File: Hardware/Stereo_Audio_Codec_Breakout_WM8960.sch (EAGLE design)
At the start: 63 parts, among them J1 QWIIC, U4 WM8960, U5 LM1117, Y1 24 MHz

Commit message: moved pwr led into sch frame
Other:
- note removed: "Power LED"
- moved on the sheet: D1, LED, R5

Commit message: Switched MONO OUT to OUT3, because that is a better name
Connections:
- removed net MONO_OUT: J3.8, U4.MONO_OUT
- new net OUT3: J3.8, U4.OUT3
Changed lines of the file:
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@@
 </segment>
 </net>
-<net name="MONO_OUT" class="0">
+<net name="OUT3" class="0">
 <segment>
-<pinref part="U4" gate="G$1" pin="MONO_OUT"/>
+<pinref part="U4" gate="G$1" pin="OUT3"/>
 <wire x1="114.3" y1="154.94" x2="116.84" y2="154.94" width="0.1524" layer="91"/>
 <label x="116.84" y="154.94" size="1.27" layer="95" font="vector" xref="yes"/>

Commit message: Switched to single GND plane
-moved to smaller vreg for AVDD
-changed how power jumpers selection and isolation works
-created 3.3V and AVDD polygons on inner layers
-increased header length to allow for 100% analog pins to be on same side.
-split SPKVDD decoupling cap into two separate 4.7uF caps and put near IC pins
-added 10 ohm in series resistors on all data lines.
-moved input filtering passives closer to IC pins
-moved SPK filtering passive closer to IC pins
-updated all silk
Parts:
- removed AVDD: JUMPER-SMT_3_1-NC_TRACE_SILK, SparkFun-Jumpers:JUMPER-SMT_3_1-NC_TRACE_SILK
- removed C11: 10uF, SparkFun-Capacitors:10UF-0805-25V-10%
- removed C2: 10uF, SparkFun-Capacitors:10UF-0402T-6.3V-20%
- removed FB1, FB2, FB3: 600Ω, SparkFun-Coils:FERRITE_BEAD-0805-600Ω-100MHZ
- removed FRAME2: FRAME-LETTER, SparkFun-Aesthetics:FRAME-LETTER
- removed J2, J3: (no value), SparkFun-Connectors:CONN_14NO_SILK
- removed R11: 240, SparkFun-Resistors:240OHM-0603-1/10W-1%
- removed U5: LM1117, SparkFun-IC-Power:V_REG_LM1117SOT223
- added AVDD-ISO: JUMPER-SMT_2_NC_TRACE_SILK, SparkFun-Jumpers:JUMPER-SMT_2_NC_TRACE_SILK
- added C12: 1.0uF, SparkFun-Capacitors:1.0UF-0402T-16V-10%
- added C14, C31: 10uF, SparkFun-Capacitors:10UF-0402T-6.3V-20%
- added C6, C7: 4.7uF, SparkFun-Capacitors:4.7UF0603
- added FRAME1: FRAME-LEDGER, SparkFun-Aesthetics:FRAME-LEDGER
- added J4, J5: (no value), SparkFun-Connectors:CONN_161X16_NO_SILK
- added R13, R14, R15, R16, R17: 10Ω, SparkFun-Resistors:10OHM-0402-1/16W-5%
- added R18: 100k, SparkFun-Resistors:100KOHM-0402T-1/16W-1%
- added U3: XC6222B331MR-G, SparkFun-IC-Power:XC6222B331MR-G
- I2C: value JUMPER-SMT_3_2-NC_TRACE_NO-SILK -> JUMPER-SMT_3_2-NC_TRACE_SILK; device SparkFun-Jumpers:JUMPER-SMT_3_2-NC_TRACE_NO-SILK -> SparkFun-Jumpers:JUMPER-SMT_3_2-NC_TRACE_SILK
- LOGO1: value SFE_LOGO_NAME_FLAMEBLANK -> SFE_LOGO_NAME_FLAME.1_INCH; device SparkFun-Aesthetics:SFE_LOGO_NAME_FLAMEBLANK -> SparkFun-Aesthetics:SFE_LOGO_NAME_FLAME.1_INCH
- R10: value 390 -> 10Ω; device SparkFun-Resistors:390OHM-0603-1/10W-1% -> SparkFun-Resistors:10OHM-0402-1/16W-5%
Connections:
- removed net AGND: C1.2, C10.1, C15.2, C16.2, C17.2, C18.2, C2.2, C21.2, C22.2, C27.2, C28.2, C29.2, C30.2, C8.1, C9.1, FB1.1, J2.11, J3.6, R10.1, U4.AGND, U4.GNDPADDLE
- removed net DGND: C11.2, C13.2, C3.1, C4.1, C5.1, FB1.2, J1.1, J2.1, R5.1, U4.DGND, U4.SPKGND1, U4.SPKGND2, Y1.GND
- removed net N$45: C1.1, FB2.2, U5.IN
- new net EN: J4.3, R18.2, U3.EN
- new net GND: C1.2, C10.1, C12.2, C13.2, C14.2, C15.2, C16.2, C17.2, C18.2, C21.2, C22.2, C27.2, C28.2, C29.2, C3.1, C30.2, C31.2, C4.1, C5.1, C6.2, C7.2, C8.1, C9.1, J1.1, J4.1, J4.16, J4.2, J4.6, J5.16, R5.1, U3.GND, U4.AGND, U4.DGND, U4.GNDPADDLE, U4.SPKGND1, U4.SPKGND2, Y1.GND
- new net N$21: R14.2, U4.DACLRC
- new net N$22: R15.2, U4.BCLK
- new net N$23: R16.2, U4.ADCDAT
- new net N$24: R17.2, U4.DACDAT
- net 3.3V: now also J4.8, SPKVDD.1; no longer FB3.2, J2.2, SPKVDD.3
- net ADCDAT: now also J4.11, R16.1; no longer J2.5, U4.ADCDAT
- net ADCLRC: now also J4.12, R13.1; no longer J2.6, U4.ADCLRC/GPIO
- net AVDD: now also AVDD-ISO.2, J5.5; no longer AVDD.2, J3.10
- net AVDD-REG: now also AVDD-ISO.1, C12.1, C14.1, U3.OUT; no longer AVDD.3, C2.1, R11.2, U5.OUT
- net BCLK: now also J4.15, R15.1; no longer J2.9, U4.BCLK
- net DACDAT: now also J4.13, R17.1; no longer J2.7, U4.DACDAT
- net DACLRC: now also J4.14, R14.1; no longer J2.8, U4.DACLRC
- net HP_L: now also J5.8; no longer J3.9
- net HP_R: now also J5.6; no longer J3.7
- net LINPUT1: now also J5.12; no longer J3.14
- net LINPUT2: now also J5.11; no longer J3.13
- net LINPUT3: now also J5.10; no longer J3.12
- net MICBIAS: now also J5.9; no longer J3.11
- net N$11: now also R10.1; no longer U4.MCLK
- net N$2: now also R13.2, U4.ADCLRC/GPIO; no longer AVDD.1, FB3.1
- net N$25: now also U4.MCLK; no longer R11.1, U5.ADJ
- net OUT3: now also J5.7; no longer J3.8
- net RINPUT1: now also J5.13; no longer J2.14
- net RINPUT2: now also J5.14; no longer J2.13
- net RINPUT3: now also J5.15; no longer J2.12
- net SCL: now also J4.10; no longer J2.4
- net SDA: now also J4.9; no longer J2.3
- net SPKVDD: now also C6.1, C7.1, J4.5; no longer C11.1, J3.1
- net SPK_LN: now also J5.3; no longer J3.4
- net SPK_LP: now also J5.4; no longer J3.5
- net SPK_RN: now also J5.1; no longer J3.2
- net SPK_RP: now also J5.2; no longer J3.3
- net VIN: now also C1.1, C31.1, J4.4, R18.1, SPKVDD.3, U3.IN; no longer FB2.1, J2.10, SPKVDD.1
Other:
- note added: "700mA out 6V max in"
- note added: "Cut AVDD-ISO Jumper To isolate AVDD from U3, And then provide AVDD at header pin."
- note added: "Power LED"
- note added: "Speaker VDD Source Selection Jumper"
- note added: "Supply Voltage Ranges VIN: 3.7-5.5V* DCVDD: 1.7-3.6V DBVDD: 1.7-3.6V AVDD: 2.7-3.6V SPKVDD: 2.7-5.5V * If VIN is used for SPKVDD, then VIN shouold be limited to 5.5V by SPKVDD max range"
- note added: "Use SPKVDD Jumper To select SPKVDD source. Leave both open to provide external SPKVDD at Header pin."
- note removed: "Power Selection Jumpers"
- note removed: "Supply Voltage Ranges DCVDD: 1.7-3.6V DBVDD: 1.7-3.6V AVDD: 2.7-3.6V SPKVDD: 2.7-5.5V"
- moved on the sheet: C1, C10, C13, C15, C16, C17, C18, C19, C20, C21, C22, C23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

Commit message: checklist catches - eng run
-Connected header pin (J4/7) to GND
-Added 4-layer board 1/2/3/4 in copper
-added ordering instructions
-added Selective solder path and moved some resistors to provide clearance on medium nozzle
-nudges some Vias to avoid cutting into silk
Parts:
- added LOGO5: SPECIAL_INSTRUCTIONS-ORDERING, SparkFun-Aesthetics:SPECIAL_INSTRUCTIONS-ORDERING
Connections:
- net GND: now also J4.7
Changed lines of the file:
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@@
 <part name="SUPPLY7" library="SparkFun-PowerSymbols" deviceset="3.3V" device=""/>
 <part name="FRAME1" library="SparkFun-Aesthetics" deviceset="FRAME-LEDGER" device=""/>
+<part name="LOGO5" library="SparkFun-Aesthetics" deviceset="SPECIAL_INSTRUCTIONS" device="-ORDERING"/>
 </parts>
 <sheets>
@@
 <attribute name="REV" x="419.1" y="6.604" size="2.7432" layer="94" font="vector"/>
 </instance>
+<instance part="LOGO5" gate="G$1" x="281.94" y="22.86" smashed="yes"/>
 </instances>
 <busses>
@@
 <wire x1="66.04" y1="101.6" x2="63.5" y2="101.6" width="0.1524" layer="91"/>
 <junction x="66.04" y="76.2"/>
-<wire x1="66.04" y1="76.2" x2="66.04" y2="101.6" width="0.1524" layer="91"/>
+<wire x1="66.04" y1="76.2" x2="66.04" y2="78.74" width="0.1524" layer="91"/>
+<wire x1="66.04" y1="78.74" x2="66.04" y2="101.6" width="0.1524" layer="91"/>
 <wire x1="66.04" y1="63.5" x2="63.5" y2="63.5" width="0.1524" layer="91"/>
 <junction x="66.04" y="63.5"/>
@@
 <wire x1="66.04" y1="66.04" x2="63.5" y2="66.04" width="0.1524" layer="91"/>
 <junction x="66.04" y="66.04"/>
-</segment>
-<segment>
+<pinref part="J4" gate="G$1" pin="7"/>
+<wire x1="66.04" y1="78.74" x2="63.5" y2="78.74" width="0.1524" layer="91"/>
+<junction x="66.04" y="78.74"/>
+</segment>
+<segment>

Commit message: corrected typo in sch note about I2C pullup jumper
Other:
- note added: "Cut I2C Jumpers to remove pullup resistors from the I2C bus."
- note removed: "Cut I2C Jumper to remove pullup jumpers from the I2C bus."
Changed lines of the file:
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@@
 <text x="348.742" y="11.43" size="2.54" layer="94" font="vector">Pete Lewis</text>
 <text x="7.62" y="271.78" size="3.81" layer="94" font="vector" ratio="10">Audio Codec</text>
-<text x="370.84" y="106.68" size="1.778" layer="97" font="vector">Cut I2C Jumper to
-remove pullup jumpers
+<text x="370.84" y="106.68" size="1.778" layer="97" font="vector">Cut I2C Jumpers to
+remove pullup resistors
 from the I2C bus.</text>
 <text x="421.64" y="7.62" size="2.54" layer="94" font="vector">v01</text>

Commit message: Silk updates and codec package update
-corrected the I2S pins to be rounded flags (because they can be inputs or outputs)
-extended pads on codec FP to allow for better fillets. (also increased roundness of pads)
-corrected I2C address in schematic to 0x1A
-bumped version to v10
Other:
- note added: "I2C Address: 0x1A (unshifted)"
- note added: "v10"
- note removed: "I2C Address: 0x34 (unshifted)"
- note removed: "v01"
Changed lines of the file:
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@@
 remove pullup resistors
 from the I2C bus.</text>
-<text x="421.64" y="7.62" size="2.54" layer="94" font="vector">v01</text>
+<text x="421.64" y="7.62" size="2.54" layer="94" font="vector">v10</text>
 <text x="331.978" y="6.858" size="1.778" layer="94" font="vector">Based on the Top pHAT by Andy England</text>
-<text x="76.708" y="169.418" size="1.778" layer="97" font="vector">I2C Address: 0x34 (unshifted)</text>
+<text x="76.708" y="169.418" size="1.778" layer="97" font="vector">I2C Address: 0x1A (unshifted)</text>
 <text x="238.76" y="93.98" size="1.27" layer="97" font="vector">Cut LED Jumper
 to disable power LED</text>

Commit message: replaced C6 and C7 to use proper SFE libraries
-Also updated tCream on codec footprint
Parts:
- C6, C7: device SparkFun-Capacitors:4.7UF0603 -> SparkFun-Capacitors:4.7UF-0603-6.3V-(10%)
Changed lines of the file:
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@@
 <part name="SUPPLY14" library="SparkFun-PowerSymbols" deviceset="5V" device="" value="SPKVDD"/>
 <part name="LOGO1" library="SparkFun-Aesthetics" deviceset="SFE_LOGO_NAME_FLAME" device=".1_INCH" value="SFE_LOGO_NAME_FLAME.1_INCH"/>
-<part name="C6" library="SparkFun-Capacitors" library_urn="urn:adsk.eagle:library:510" deviceset="4.7UF" device="0603" package3d_urn="urn:adsk.eagle:package:37414/1" value="4.7uF"/>
-<part name="C7" library="SparkFun-Capacitors" library_urn="urn:adsk.eagle:library:510" deviceset="4.7UF" device="0603" package3d_urn="urn:adsk.eagle:package:37414/1" value="4.7uF"/>
+<part name="C6" library="SparkFun-Capacitors" deviceset="4.7UF" device="-0603-6.3V-(10%)" value="4.7uF"/>
+<part name="C7" library="SparkFun-Capacitors" deviceset="4.7UF" device="-0603-6.3V-(10%)" value="4.7uF"/>
 <part name="R13" library="SparkFun-Resistors" deviceset="10OHM" device="-0402-1/16W-5%" value="10Ω"/>
 <part name="R14" library="SparkFun-Resistors" deviceset="10OHM" device="-0402-1/16W-5%" value="10Ω"/>
@@
 which will not be processed correctly with this version.
 </note>
-<note version="8.2" severity="warning">
-Since Version 8.2, EAGLE supports online libraries. The ids
-of those online libraries will not be understood (or retained)
-with this version.
-</note>
 <note version="8.3" severity="warning">

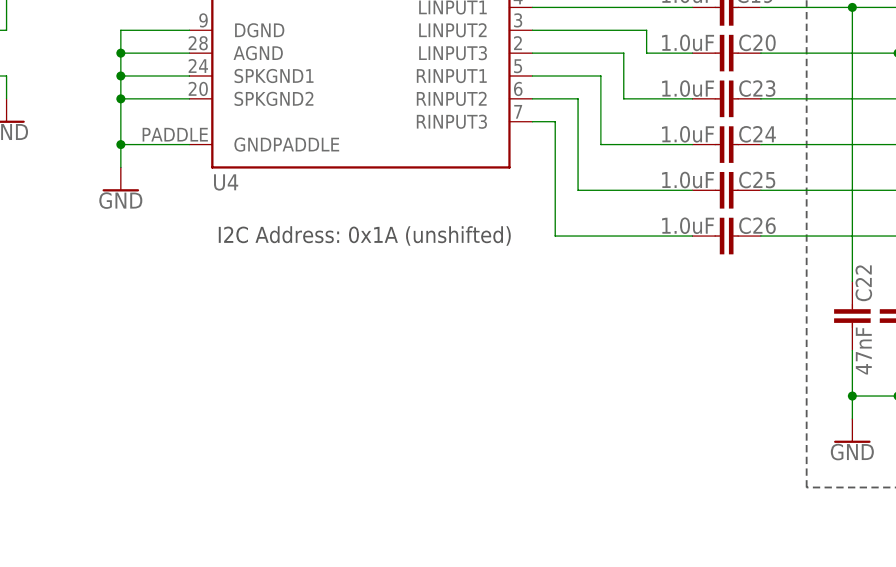
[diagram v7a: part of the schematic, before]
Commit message: Moved fiducials to avoid silk overlap
-also increase I2C address text size in sch
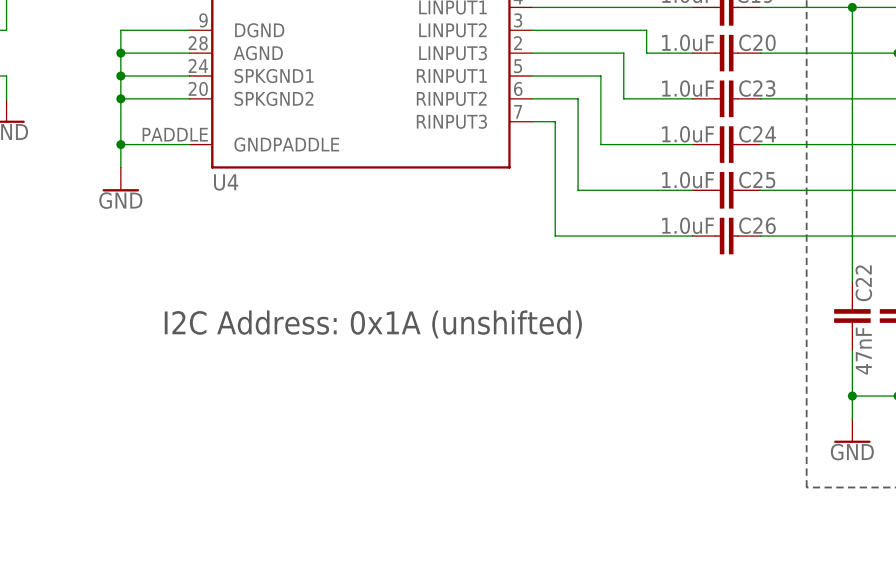
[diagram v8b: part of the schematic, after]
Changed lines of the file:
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@@
 <text x="421.64" y="7.62" size="2.54" layer="94" font="vector">v10</text>
 <text x="331.978" y="6.858" size="1.778" layer="94" font="vector">Based on the Top pHAT by Andy England</text>
-<text x="76.708" y="169.418" size="1.778" layer="97" font="vector">I2C Address: 0x1A (unshifted)</text>
+<text x="70.612" y="159.258" size="2.54" layer="97" font="vector" ratio="10">I2C Address: 0x1A (unshifted)</text>
 <text x="238.76" y="93.98" size="1.27" layer="97" font="vector">Cut LED Jumper
 to disable power LED</text>
